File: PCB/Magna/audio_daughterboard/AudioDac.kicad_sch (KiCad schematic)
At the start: 44 parts, among them U401 NE5532, U403 PCM1789

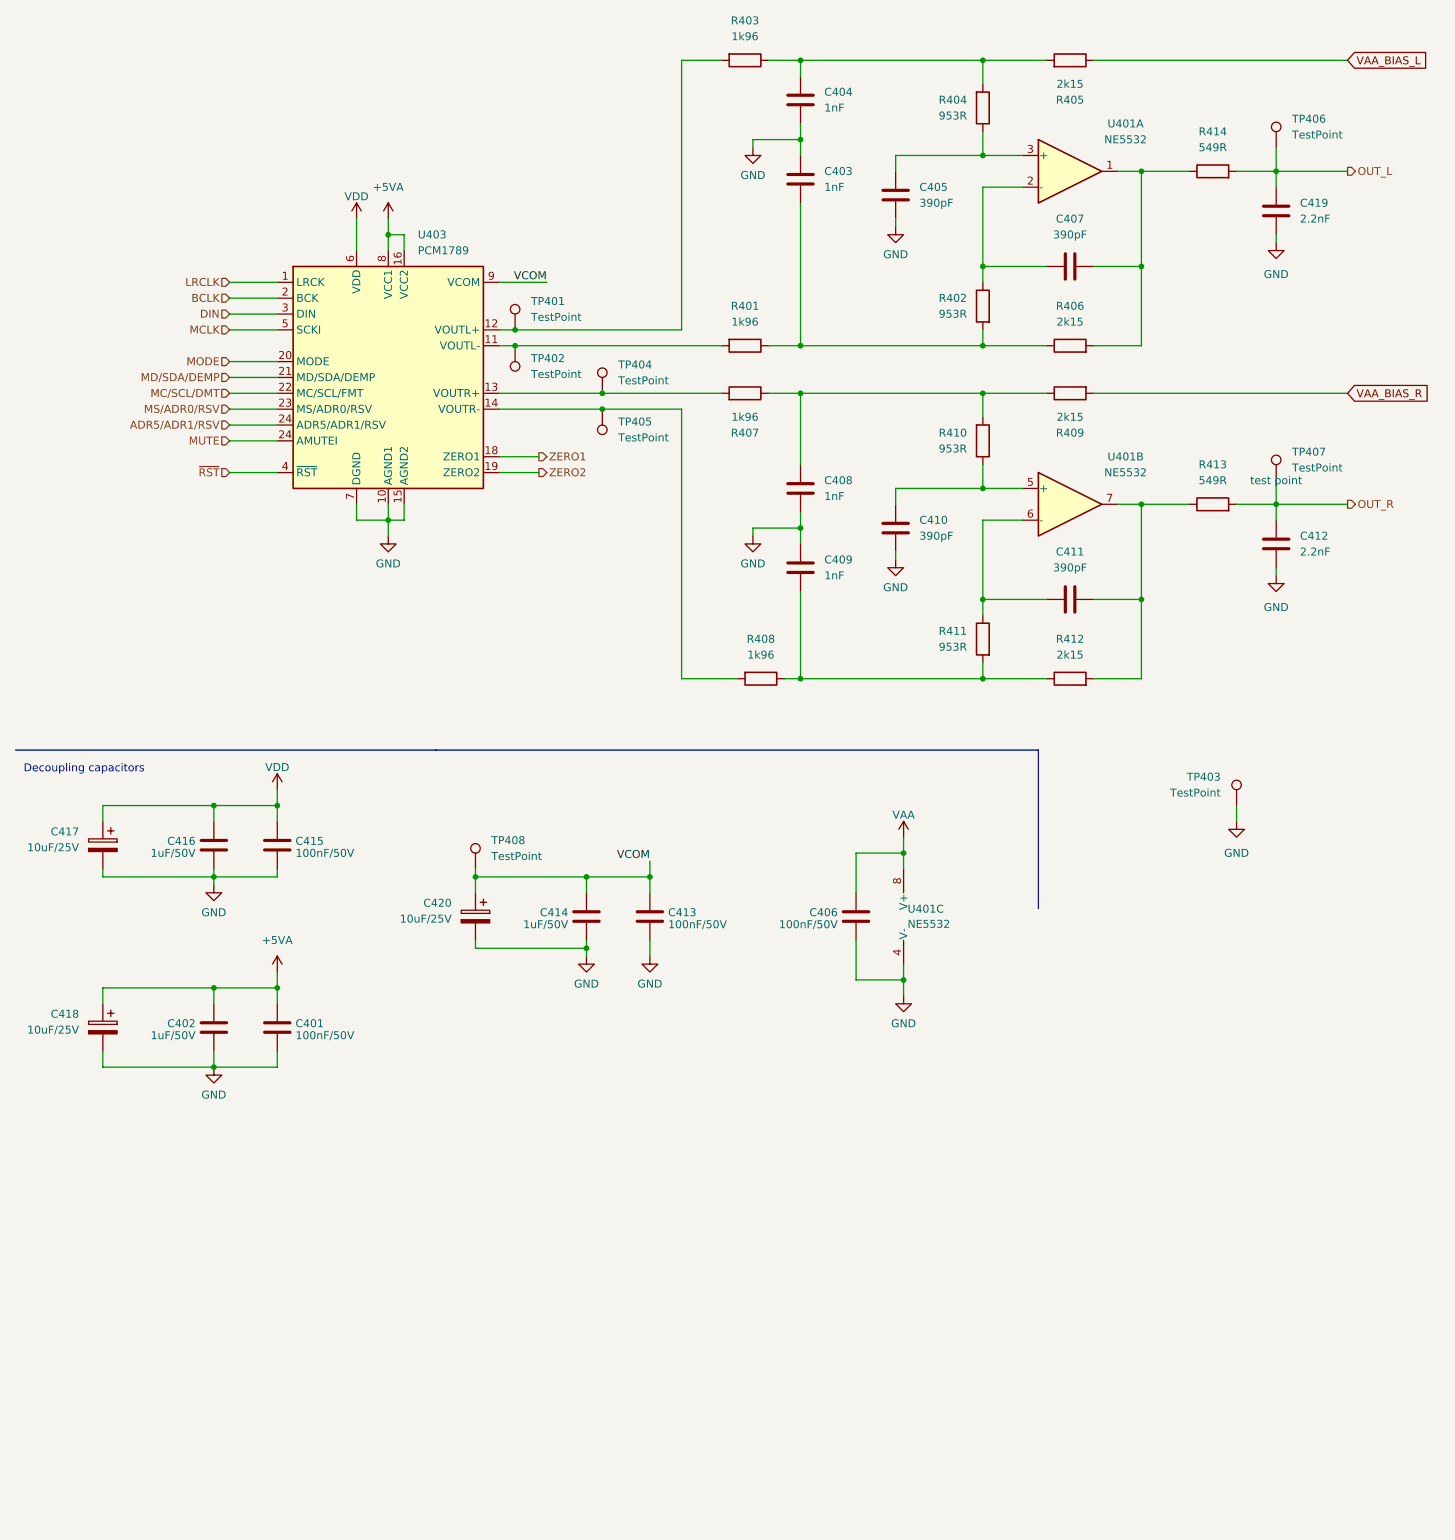
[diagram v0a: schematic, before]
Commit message: Update audio PCB
Mainly added simulations to Linedriver and DAC.

Also fixed some small issues that was found when simulating
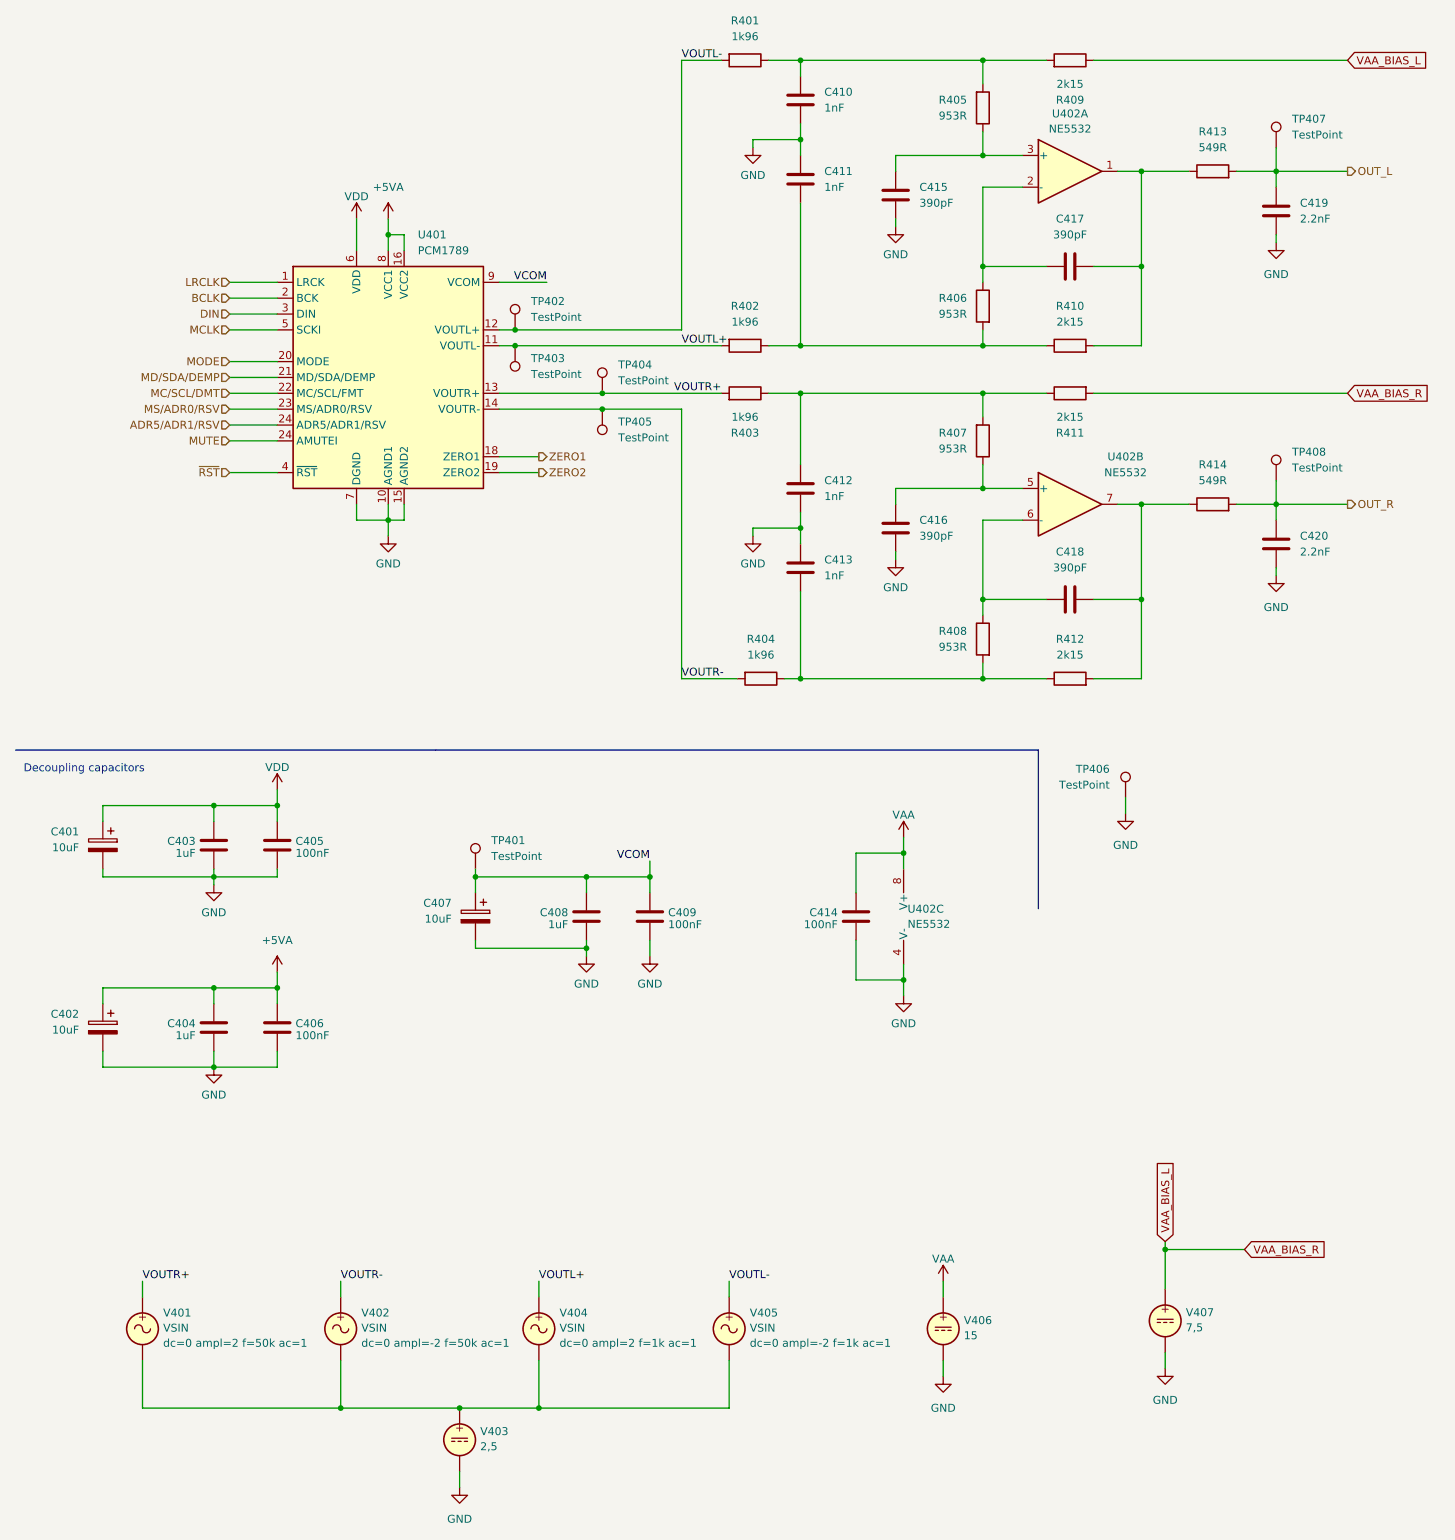
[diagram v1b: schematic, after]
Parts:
- removed unit 1 of U401
- added unit 1 of U402
- added V401, V402, V404, V405: VSIN, symbol Simulation_SPICE:VSIN
- added V403: 2,5, symbol Simulation_SPICE:VDC
- added V406: 15, symbol Simulation_SPICE:VDC
- added V407: 7,5, symbol Simulation_SPICE:VDC
- C401: renamed from C417; value 10uF/25V -> 10uF
- C402: renamed from C418; value 10uF/25V -> 10uF
- C403: renamed from C416; value 1uF/50V -> 1uF
- C404: renamed from C402; value 1uF/50V -> 1uF
- C405: renamed from C415; value 100nF/50V -> 100nF
- C406: renamed from C401; value 100nF/50V -> 100nF
- C407: renamed from C420; value 10uF/25V -> 10uF
- C408: renamed from C414; value 1uF/50V -> 1uF
- C409: renamed from C413; value 100nF/50V -> 100nF
- C414: renamed from C406; value 100nF/50V -> 100nF
- renumbered C404 to C410, C403 to C411, C408 to C412, C409 to C413, C405 to C415, C410 to C416, C407 to C417, C411 to C418, C412 to C420, R403 to R401, R401 to R402, R407 to R403, R408 to R404, R404 to R405, R402 to R406, R410 to R407, R411 to R408, R405 to R409, R406 to R410, R409 to R411, R414 to R413, R413 to R414, TP408 to TP401, TP401 to TP402, TP402 to TP403, TP403 to TP406, TP406 to TP407, TP407 to TP408, U403 to U401, U401 to U402
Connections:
- net VAA_BIAS_R is gone; now on net VAA_BIAS_L: R411.2
- net GND: now also V403.2, V406.2, V407.2
- net VAA: now also V406.1
- net VAA_BIAS_L: now also V407.1
- net at C417.2, R410.2, R413.1: now also U402.1
- net at C417.1, R406.1: now also U402.2 (-)
- net at C415.1, R405.1: now also U402.3 (+)
- net VOUTL-: now reaches R401.2, TP402.1, U401.12 (VOUTL+)
- net VOUTL-: now also V405.1
- net VOUTR-: now reaches R404.2, TP405.1, U401.14 (VOUTR-)
- net VOUTR-: now also V402.1
- net VOUTL+: now reaches R402.2, TP403.1, U401.11 (VOUTL-)
- net VOUTL+: now also V404.1
- net VOUTR+: now reaches R403.2, TP404.1, U401.13 (VOUTR+)
- net VOUTR+: now also V401.1
- new net: V401.2, V402.2, V403.1, V404.2, V405.2
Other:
- moved on the sheet: TP406

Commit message: "Finalize" Audio daugherboard
Finished DAC output filter
Fixed the whole damn MCU subschematic
Fixed Linedriver schematic
Added component footprints and LCSC numbers
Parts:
- removed V402: VSIN, symbol Simulation_SPICE:VSIN
- removed V403: 2,5, symbol Simulation_SPICE:VDC
- added C411, C412, C414, C415: 100u, Capacitor_SMD:CP_Elec_6.3x5.8, symbol Device:C_Polarized
- added C413: 100nF, Capacitor_SMD:C_0805_2012Metric_Pad1.18x1.45mm_HandSolder, symbol Device:C
- added R401, R402, R403, R404: 22k, Resistor_SMD:R_0603_1608Metric, symbol Device:R
- added TP407, TP408, TP409, TP410: TestPoint, TestPoint:TestPoint_Keystone_5005-5009_Compact, symbol Connector:TestPoint
- added U403: NE5532, Package_SO:SOIC-8_3.9x4.9mm_P1.27mm, symbol Amplifier_Operational:NE5532
- added V401: 2.5, symbol Simulation_SPICE:VDC
- added V403: VSIN, symbol Simulation_SPICE:VSIN
- added V407: 7,5, symbol Simulation_SPICE:VDC
- C401, C403, C405, V404, V405, V406: now left out of the parts list
- C402: renamed from C407; now left out of the parts list
- C404: renamed from C408; now left out of the parts list
- C406: renamed from C409; now left out of the parts list
- C407: renamed from C402; now left out of the parts list
- C408: renamed from C404; now left out of the parts list
- C409: renamed from C406; now left out of the parts list
- C410: renamed from C414; now left out of the parts list
- C416: renamed from C410; footprint (none) -> Capacitor_SMD:C_0603_1608Metric; LCSC (none) -> C163508; now left out of the parts list
- C417: renamed from C411; footprint (none) -> Capacitor_SMD:C_0603_1608Metric; LCSC (none) -> C163508; now left out of the parts list
- C418: renamed from C412; footprint (none) -> Capacitor_SMD:C_0603_1608Metric; LCSC (none) -> C163508; now left out of the parts list
- C419: renamed from C413; footprint (none) -> Capacitor_SMD:C_0603_1608Metric; LCSC (none) -> C163508; now left out of the parts list
- C420: renamed from C415; footprint (none) -> Capacitor_SMD:C_0603_1608Metric; LCSC (none) -> C472793; now left out of the parts list
- C421: renamed from C416; footprint (none) -> Capacitor_SMD:C_0603_1608Metric; LCSC (none) -> C472793; now left out of the parts list
- C422: renamed from C417; footprint (none) -> Capacitor_SMD:C_0603_1608Metric; LCSC (none) -> C472793; now left out of the parts list
- C423: renamed from C418; footprint (none) -> Capacitor_SMD:C_0603_1608Metric; LCSC (none) -> C472793; now left out of the parts list
- C424: renamed from C419; footprint (none) -> Capacitor_SMD:C_0603_1608Metric; LCSC (none) -> CL10C222JB8NNNC; now left out of the parts list
- C425: renamed from C420; footprint (none) -> Capacitor_SMD:C_0603_1608Metric; LCSC (none) -> CL10C222JB8NNNC; now left out of the parts list
- R405: renamed from R401; footprint (none) -> Resistor_SMD:R_0603_1608Metric; LCSC (none) -> C160602; now left out of the parts list
- R406: renamed from R402; footprint (none) -> Resistor_SMD:R_0603_1608Metric; LCSC (none) -> C160602; now left out of the parts list
- R407: renamed from R403; footprint (none) -> Resistor_SMD:R_0603_1608Metric; LCSC (none) -> C160602; now left out of the parts list
- R408: renamed from R404; footprint (none) -> Resistor_SMD:R_0603_1608Metric; LCSC (none) -> C160602; now left out of the parts list
- R409: renamed from R405; footprint (none) -> Resistor_SMD:R_0603_1608Metric; LCSC (none) -> C311896; now left out of the parts list
- R410: renamed from R406; footprint (none) -> Resistor_SMD:R_0603_1608Metric; LCSC (none) -> C311896; now left out of the parts list
- R411: renamed from R407; footprint (none) -> Resistor_SMD:R_0603_1608Metric; LCSC (none) -> C311896; now left out of the parts list
- R412: renamed from R408; footprint (none) -> Resistor_SMD:R_0603_1608Metric; LCSC (none) -> C311896; now left out of the parts list
- R413: renamed from R409; footprint (none) -> Resistor_SMD:R_0603_1608Metric; LCSC (none) -> C667562; now left out of the parts list
- R414: renamed from R410; footprint (none) -> Resistor_SMD:R_0603_1608Metric; LCSC (none) -> C667562; now left out of the parts list
- R415: renamed from R411; footprint (none) -> Resistor_SMD:R_0603_1608Metric; LCSC (none) -> C667562; now left out of the parts list
- R416: renamed from R412; footprint (none) -> Resistor_SMD:R_0603_1608Metric; LCSC (none) -> C667562; now left out of the parts list
- R417: renamed from R413; footprint (none) -> Resistor_SMD:R_0603_1608Metric; LCSC (none) -> C218072; now left out of the parts list
- R418: renamed from R414; footprint (none) -> Resistor_SMD:R_0603_1608Metric; LCSC (none) -> C218072; now left out of the parts list
- TP401: footprint (none) -> TestPoint:TestPoint_Keystone_5005-5009_Compact; now left out of the parts list
- TP402: renamed from TP406; now left out of the parts list
- TP403: renamed from TP404; footprint (none) -> TestPoint:TestPoint_Keystone_5005-5009_Compact; now left out of the parts list
- TP404: renamed from TP405; footprint (none) -> TestPoint:TestPoint_Keystone_5005-5009_Compact; now left out of the parts list
- TP405: renamed from TP402; footprint (none) -> TestPoint:TestPoint_Keystone_5005-5009_Compact; now left out of the parts list
- TP406: renamed from TP403; footprint (none) -> TestPoint:TestPoint_Keystone_5005-5009_Compact; now left out of the parts list
- TP411: renamed from TP407; footprint (none) -> TestPoint:TestPoint_Keystone_5005-5009_Compact; now left out of the parts list
- TP412: renamed from TP408; footprint (none) -> TestPoint:TestPoint_Keystone_5005-5009_Compact; now left out of the parts list
- U401: LCSC (none) -> C962089; now left out of the parts list
- U402: footprint (none) -> Package_SO:SOIC-8_3.9x4.9mm_P1.27mm; LCSC (none) -> C7426; now left out of the parts list
- V402: renamed from V401; now left out of the parts list
- V408: renamed from V407; now left out of the parts list
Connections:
- net GND: now also C413.2, U403.4 (V-), V401.2, V407.2
- net MUTE: now also U401.17 (AMUTEI); no longer U401.24 (AMUTEI)
- net OUT_L: now also U403.1, U403.2 (-); no longer C424.2, R417.2, TP411.1
- net OUT_R: now also U403.6 (-), U403.7; no longer C425.2, R418.2, TP412.1
- net VAA: now also C413.1, U403.8 (V+)
- net VAA_BIAS_L: now also R401.1, R403.1, V407.1; no longer R415.2, V408.1
- net VCOM: now also V402.2, V404.2, V405.1, V401.1, V403.1
- net VOUTL+: now also TP405.1, U401.12 (VOUTL+), C411.2; no longer R406.2, TP406.1, U401.11 (VOUTL-)
- net VOUTL-: now also TP406.1, U401.11 (VOUTL-), V405.2, C414.2; no longer R405.2, TP405.1, U401.12 (VOUTL+), V405.1
- net VOUTR+: now also C412.2; no longer R407.2
- net VOUTR-: now also C415.2, V403.2; no longer R408.2
- new net LEFT_FILTERED: C424.2, R417.2, TP411.1, U403.3 (+)
- new net RIGHT_FILTERED: C425.2, R418.2, TP412.1, U403.5 (+)
- new net VAA_BIAS_R: R402.1, R404.1, R415.2, V408.1
- new net VOUTL+_BIASED: C411.1, R401.2, R405.2, TP409.1
- new net VOUTL-_BIASED: C414.1, R403.2, R406.2, TP410.1
- new net VOUTR+_BIASED: C412.1, R404.2, R407.2, TP407.1
- new net VOUTR-_BIASED: C415.1, R402.2, R408.2, TP408.1
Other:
- note added: ".tran 1u 1m uic .ic V(VOUTL+_BIASED)=7.5 .ic V(VOUTL-_BIASED)=7.5 .ic V(VOUTR+_BIASED)=7.5 .ic V(VOUTR-_BIASED)=7.5"
- note added: "Anti aliasing lowpass filter"
- note added: "Output buffer"
- moved on the sheet: C401, C402, C403, C404, C405, C406, C407, C408, C409, C410, C416, C417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

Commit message: Do most of the component placement for audio board
Just a general layout, things will probably change
as the routing begins.
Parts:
- removed C401, C402, C407: 10uF, Capacitor_SMD:CP_Elec_4x5.8, symbol Device:C_Polarized
- removed TP401, TP403, TP404, TP411, TP412: TestPoint, TestPoint:TestPoint_Keystone_5005-5009_Compact, symbol Connector:TestPoint
- added C401, C402, C407: 4.7uF, Capacitor_SMD:C_1206_3216Metric, symbol Device:C
- added TP401, TP403, TP404, TP405, TP412: TestPoint, TestPoint:TestPoint_Pad_1.0x1.0mm, symbol Connector:TestPoint_Alt
- C403, C404, C408: value 1uF -> 4.7uF; footprint Capacitor_SMD:C_0805_2012Metric_Pad1.18x1.45mm_HandSolder -> Capacitor_SMD:C_1206_3216Metric; LCSC C28323 -> C29823; Votlage (none) -> 25V
- C405, C406, C409, C410, C413: footprint Capacitor_SMD:C_0805_2012Metric_Pad1.18x1.45mm_HandSolder -> Capacitor_SMD:C_0603_1608Metric; LCSC C49678 -> C14663
- C411, C412, C414, C415: footprint Capacitor_SMD:CP_Elec_6.3x5.8 -> Capacitor_SMD:CP_Elec_6.3x7.7; LCSC C2166157 -> C251007
- TP406: footprint TestPoint:TestPoint_Keystone_5005-5009_Compact -> TestPoint:TestPoint_Pad_1.0x1.0mm; symbol Connector:TestPoint -> Connector:TestPoint_Alt; now in the parts list
- TP411: renamed from TP405; footprint TestPoint:TestPoint_Keystone_5005-5009_Compact -> TestPoint:TestPoint_Pad_1.0x1.0mm; symbol Connector:TestPoint -> Connector:TestPoint_Alt; now in the parts list
- renumbered C418 to C416, C419 to C417, C416 to C418, C417 to C419, C421 to C420, C420 to C421, C423 to C422, C422 to C423, C425 to C424, C424 to C425, R404 to R401, R403 to R402, R402 to R403, R401 to R404, R408 to R405, R407 to R406, R406 to R407, R405 to R408, R411 to R409, R412 to R410, R409 to R411, R410 to R412, R415 to R413, R416 to R414, R413 to R415, R414 to R416, R418 to R417, R417 to R418
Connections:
- net +5VA: now also C407.1
- net GND: now also C401.2, C402.2, C407.2
- net LEFT_FILTERED: now also C424.2, R417.2, TP411.1, U403.5 (+); no longer C425.2, R418.2, U403.3 (+)
- net OUT_L: now also U403.6 (-), U403.7; no longer U403.1, U403.2 (-)
- net OUT_R: now also U403.1, U403.2 (-); no longer U403.6 (-), U403.7
- net RIGHT_FILTERED: now also C425.2, R418.2, U403.3 (+), TP412.1; no longer C424.2, R417.2, U403.5 (+)
- net VAA_BIAS_L: now also R401.1, R403.1, R413.1; no longer R402.1, R404.1, R415.1
- net VAA_BIAS_R: now also R402.1, R404.1, R415.2; no longer R401.1, R403.1, R413.2
- net VCOM: now also C402.1, TP401.1
- net VDD: now also C401.1
- net VOUTL+: now also TP405.1; no longer TP411.1
- net VOUTL+_BIASED: now also R401.2, R405.2; no longer R404.2, R408.2
- net VOUTL-_BIASED: now also R403.2, R406.2; no longer R402.2, R407.2
- net VOUTR+: now also TP403.1
- net VOUTR+_BIASED: now also R404.2, R407.2; no longer R401.2, R406.2
- net VOUTR-: now also TP404.1
- net VOUTR-_BIASED: now also R402.2, R408.2; no longer R403.2, R405.2
- net at C416.1, R409.2: now also R405.1, R413.2; no longer R406.1, R413.1
- net at C419.2, R412.2, R416.1: now also R408.1; no longer R407.1
- net at C418.1, R411.2: now also R407.1, R415.1; no longer R408.1, R415.2
- net at C417.2, R410.2, R414.1: now also R406.1; no longer R405.1
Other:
- moved on the sheet: C416, C417, C418, C419, C420, C421, C422, C423, C424, C425, R401, R402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
